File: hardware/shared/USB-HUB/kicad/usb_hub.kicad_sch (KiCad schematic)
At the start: 0 parts

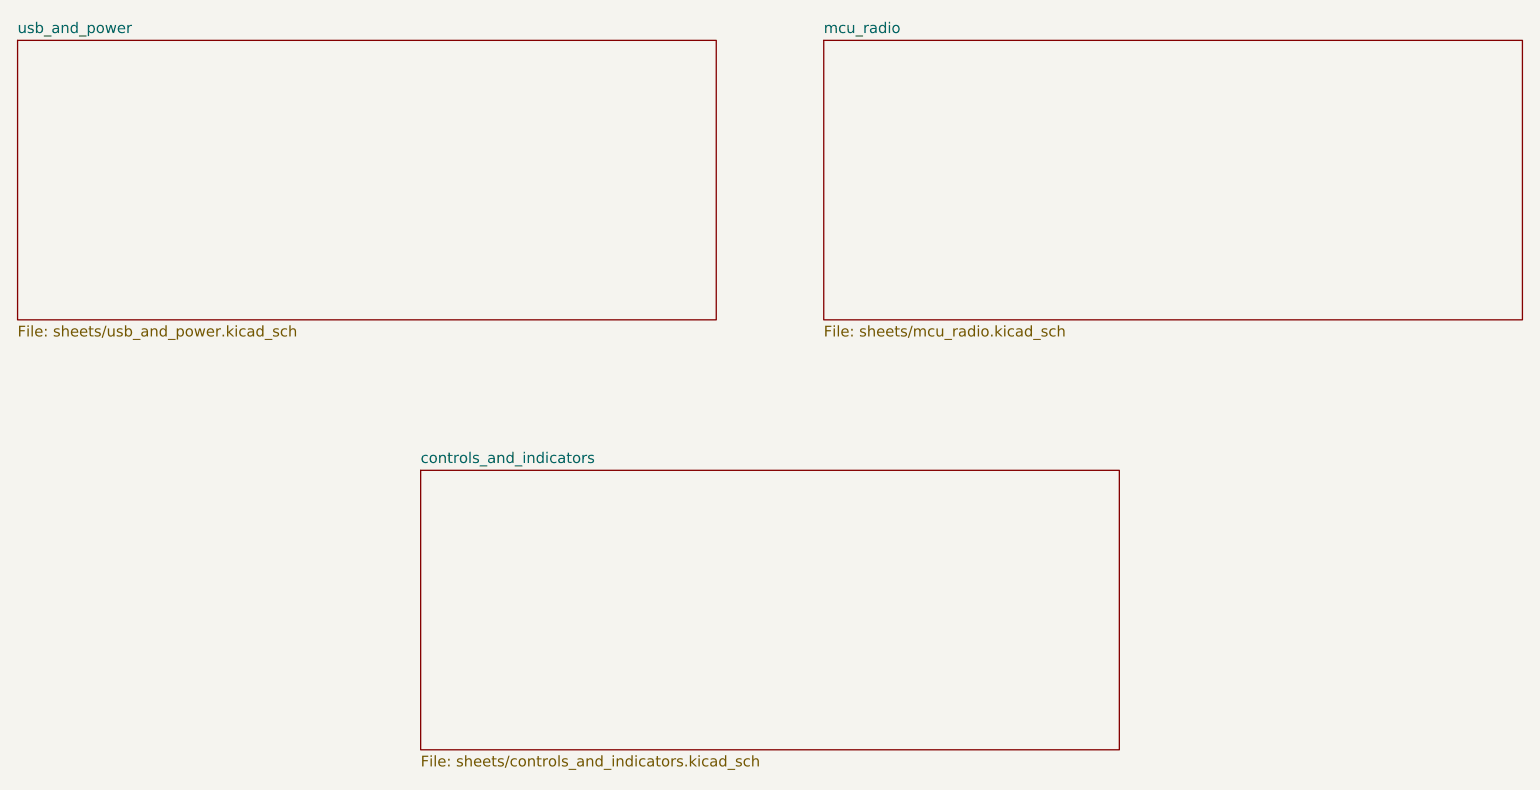
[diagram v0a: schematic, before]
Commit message: feat(hardware): wire 30deg optical ring power and hub USB interfaces for accessibility pointing, ~$9 ring / ~$5-6 hub BOM
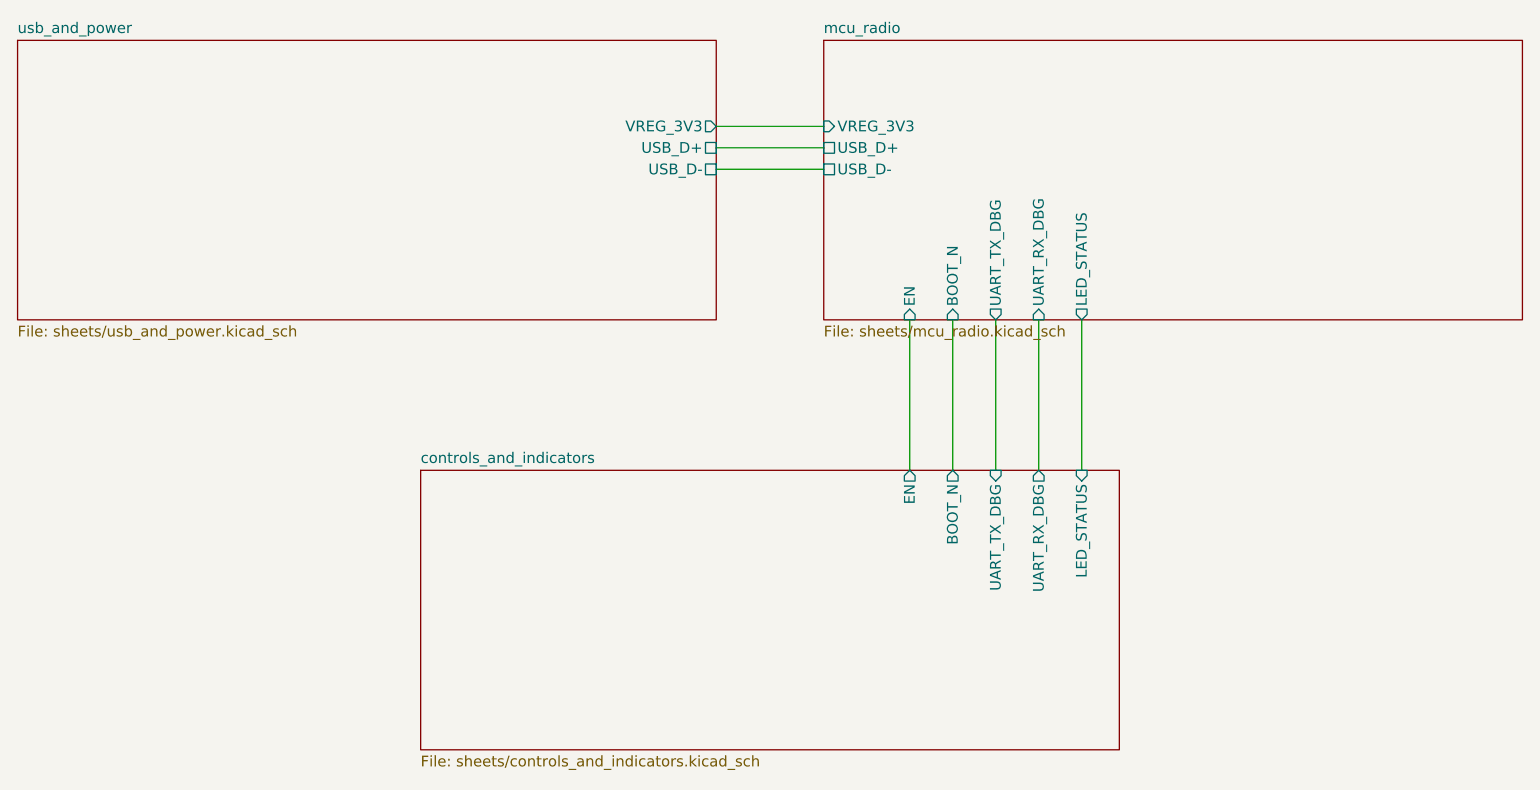
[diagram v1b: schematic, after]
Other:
- sheet controls_and_indicators ports: added BOOT_N, EN, LED_STATUS, UART_RX_DBG, UART_TX_DBG; removed none
- sheet mcu_radio ports: added BOOT_N, EN, LED_STATUS, UART_RX_DBG, UART_TX_DBG, USB_D+, USB_D-, VREG_3V3; removed none
- sheet usb_and_power ports: added USB_D+, USB_D-, VREG_3V3; removed none
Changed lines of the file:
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@@
       (effects (font (size 1.27 1.27)) (justify left top))
+    )
+    (pin "VREG_3V3" output (at 107.95 35.56 0)
+      (effects (font (size 1.27 1.27)) (justify right))
+    )
+    (pin "USB_D+" passive (at 107.95 38.1 0)
+      (effects (font (size 1.27 1.27)) (justify right))
+    )
+    (pin "USB_D-" passive (at 107.95 40.64 0)
+      (effects (font (size 1.27 1.27)) (justify right))
     )
     (instances
@@
       (effects (font (size 1.27 1.27)) (justify left top))
     )
+    (pin "VREG_3V3" input (at 120.65 35.56 180)
+      (effects (font (size 1.27 1.27)) (justify left))
+    )
+    (pin "USB_D+" passive (at 120.65 38.1 180)
+      (effects (font (size 1.27 1.27)) (justify left))
+    )
+    (pin "USB_D-" passive (at 120.65 40.64 180)
+      (effects (font (size 1.27 1.27)) (justify left))
+    )
+    (pin "EN" input (at 130.81 58.42 270)
+      (effects (font (size 1.27 1.27)))
+    )
+    (pin "BOOT_N" input (at 135.89 58.42 270)
+      (effects (font (size 1.27 1.27)))
+    )
+    (pin "UART_TX_DBG" output (at 140.97 58.42 270)
+      (effects (font (size 1.27 1.27)))
+    )
+    (pin "UART_RX_DBG" input (at 146.05 58.42 270)
+      (effects (font (size 1.27 1.27)))
+    )
+    (pin "LED_STATUS" output (at 151.13 58.42 270)
+      (effects (font (size 1.27 1.27)))
+    )
     (instances
       (project "usb_hub"
@@
       (effects (font (size 1.27 1.27)) (justify left top))
     )
+    (pin "EN" output (at 130.81 76.2 90)
+      (effects (font (size 1.27 1.27)))
+    )
+    (pin "BOOT_N" output (at 135.89 76.2 90)
+      (effects (font (size 1.27 1.27)))
+    )
+    (pin "UART_TX_DBG" input (at 140.97 76.2 90)
+      (effects (font (size 1.27 1.27)))
+    )
+    (pin "UART_RX_DBG" output (at 146.05 76.2 90)
+      (effects (font (size 1.27 1.27)))
+    )
+    (pin "LED_STATUS" input (at 151.13 76.2 90)
+      (effects (font (size 1.27 1.27)))
+    )
     (instances
       (project "usb_hub"
@@
     )
   )
+  (wire
+    (pts
+      (xy 107.95 35.56)
+      (xy 120.65 35.56)
+    )
+    (stroke (width 0) (type default) (color 0 0 0 0))
+  )
+  (wire
+    (pts
+      (xy 107.95 38.1)
+      (xy 120.65 38.1)
+    )
+    (stroke (width 0) (type default) (color 0 0 0 0))
+  )
+  (wire
+    (pts
+      (xy 107.95 40.64)
+      (xy 120.65 40.64)
+    )
+    (stroke (width 0) (type default) (color 0 0 0 0))
+  )
+  (wire
+    (pts
+      (xy 130.81 58.42)
+      (xy 130.81 76.2)
+    )
+    (stroke (width 0) (type default) (color 0 0 0 0))
+  )
+  (wire
+    (pts
+      (xy 135.89 58.42)
+      (xy 135.89 76.2)
+    )
+    (stroke (width 0) (type default) (color 0 0 0 0))
+  )
+  (wire
+    (pts
+      (xy 140.97 58.42)
+      (xy 140.97 76.2)
+    )
+    (stroke (width 0) (type default) (color 0 0 0 0))
+  )
+  (wire
+    (pts
+      (xy 146.05 58.42)
+      (xy 146.05 76.2)
+    )
+    (stroke (width 0) (type default) (color 0 0 0 0))
+  )
+  (wire
+    (pts
+      (xy 151.13 58.42)
+      (xy 151.13 76.2)
+    )
+    (stroke (width 0) (type default) (color 0 0 0 0))
+  )
   (sheet_instances

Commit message: fix(usb-hub): clean native-usb dongle drc parity
Direct-plug native USB hub dongle for accessibility pointing and OCR composition; no sensing mechanism change; BOM intent remains ~-6.
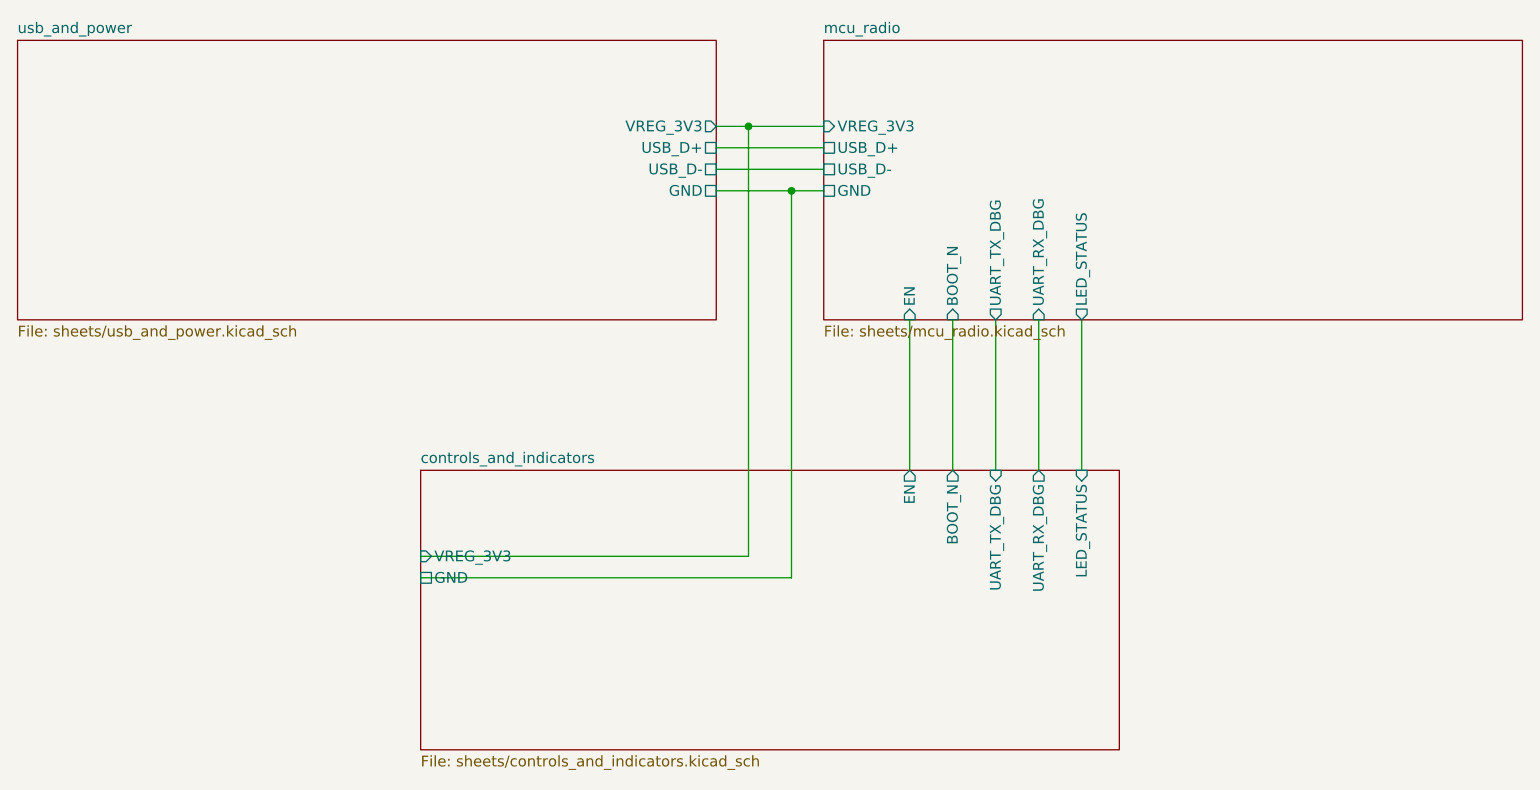
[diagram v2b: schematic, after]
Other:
- sheet controls_and_indicators ports: added GND, VREG_3V3; removed none
- sheet mcu_radio ports: added GND; removed none
- sheet usb_and_power ports: added GND; removed none
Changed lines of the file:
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@@
+      (effects (font (size 1.27 1.27)) (justify right))
+    )
+    (pin "GND" passive (at 107.95 43.18 0)
       (effects (font (size 1.27 1.27)) (justify right))
     )
@@
     )
     (pin "USB_D-" passive (at 120.65 40.64 180)
+      (effects (font (size 1.27 1.27)) (justify left))
+    )
+    (pin "GND" passive (at 120.65 43.18 180)
       (effects (font (size 1.27 1.27)) (justify left))
     )
@@
       (effects (font (size 1.27 1.27)))
     )
+    (pin "VREG_3V3" input (at 73.025 86.36 180)
+      (effects (font (size 1.27 1.27)) (justify left))
+    )
+    (pin "GND" passive (at 73.025 88.9 180)
+      (effects (font (size 1.27 1.27)) (justify left))
+    )
     (instances
       (project "usb_hub"
@@
   )
   (wire
+    (pts
+      (xy 107.95 43.18)
+      (xy 120.65 43.18)
+    )
+    (stroke (width 0) (type default) (color 0 0 0 0))
+  )
+  (wire
+    (pts
+      (xy 111.76 35.56)
+      (xy 111.76 86.36)
+    )
+    (stroke (width 0) (type default) (color 0 0 0 0))
+  )
+  (wire
+    (pts
+      (xy 111.76 86.36)
+      (xy 73.025 86.36)
+    )
+    (stroke (width 0) (type default) (color 0 0 0 0))
+  )
+  (wire
+    (pts
+      (xy 116.84 43.18)
+      (xy 116.84 88.9)
+    )
+    (stroke (width 0) (type default) (color 0 0 0 0))
+  )
+  (wire
+    (pts
+      (xy 116.84 88.9)
+      (xy 73.025 88.9)
+    )
+    (stroke (width 0) (type default) (color 0 0 0 0))
+  )
+  (junction
+    (at 111.76 35.56)
+    (diameter 0)
+    (color 0 0 0 0)
+  )
+  (junction
+    (at 116.84 43.18)
+    (diameter 0)
+    (color 0 0 0 0)
+  )
+  (wire

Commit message: fix(usb-hub): close kicad erc snapshot
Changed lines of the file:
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@@
   )
   (sheet
-    (at 73.025 76.2)
+    (at 73.66 76.2)
     (size 82.55 33.02)
     (stroke (width 0.1524) (type solid) (color 0 0 0 0))
     (fill (color 0 0 0 0.0000))
-    (property "Sheet name" "controls_and_indicators" (id 0) (at 73.025 75.4884 0)
+    (property "Sheet name" "controls_and_indicators" (id 0) (at 73.66 75.4884 0)
       (effects (font (size 1.27 1.27)) (justify left bottom))
     )
-    (property "Sheet file" "sheets/controls_and_indicators.kicad_sch" (id 1) (at 73.025 109.8546 0)
+    (property "Sheet file" "sheets/controls_and_indicators.kicad_sch" (id 1) (at 73.66 109.8546 0)
       (effects (font (size 1.27 1.27)) (justify left top))
     )
@@
       (effects (font (size 1.27 1.27)))
     )
-    (pin "VREG_3V3" input (at 73.025 86.36 180)
+    (pin "VREG_3V3" input (at 73.66 86.36 180)
       (effects (font (size 1.27 1.27)) (justify left))
     )
-    (pin "GND" passive (at 73.025 88.9 180)
+    (pin "GND" passive (at 73.66 88.9 180)
       (effects (font (size 1.27 1.27)) (justify left))
     )
@@
     (pts
       (xy 111.76 86.36)
-      (xy 73.025 86.36)
+      (xy 73.66 86.36)
     )
     (stroke (width 0) (type default) (color 0 0 0 0))
@@
     (pts
       (xy 116.84 88.9)
-      (xy 73.025 88.9)
+      (xy 73.66 88.9)
     )
     (stroke (width 0) (type default) (color 0 0 0 0))
